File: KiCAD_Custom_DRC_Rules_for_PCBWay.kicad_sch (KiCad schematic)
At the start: 38 parts, among them J1 Screw_Terminal_01x02, J2 x2 OpAmp ZIF, J3 x1 OpAmp ZIF, J4 x4 OpAmp ZIF, U1 TL072

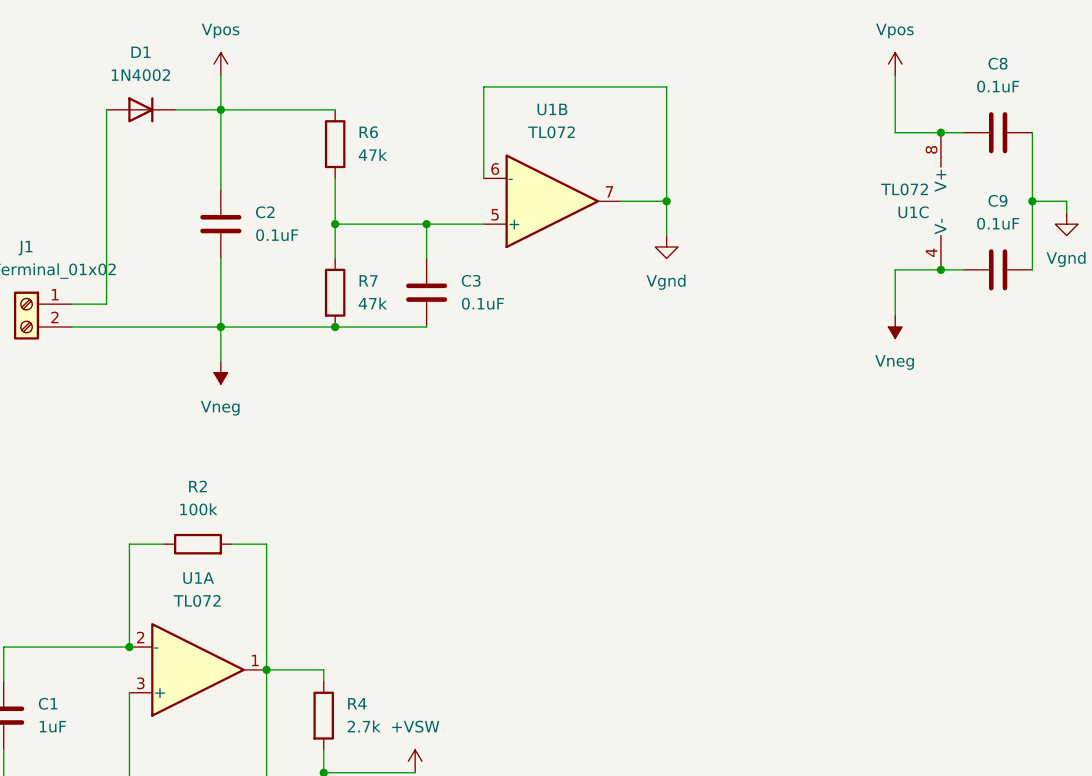
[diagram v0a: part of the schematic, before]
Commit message: cleanup, datasheet updates, add BOM
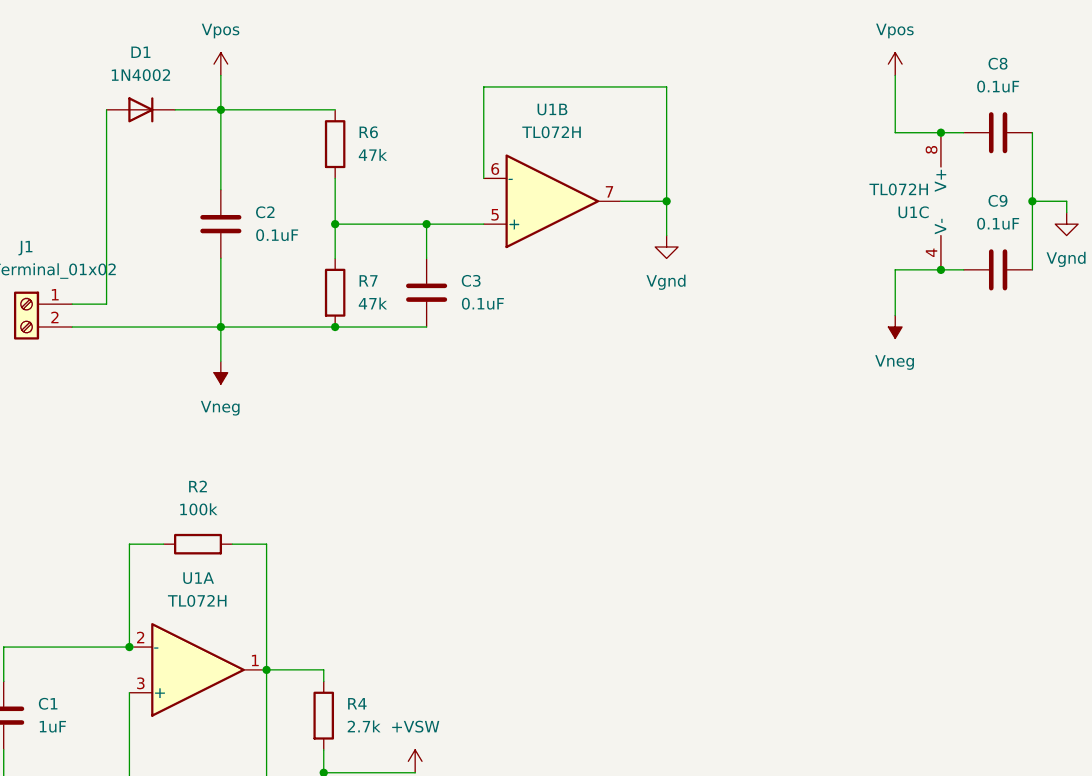
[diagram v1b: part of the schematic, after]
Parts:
- U1: value TL072 -> TL072H
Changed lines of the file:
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@@
 			)
 		)
-		(property "Value" "TL072"
+		(property "Value" "TL072H"
 			(at 82.55 26.67 0)
 			(effects
@@
 			)
 		)
-		(property "Datasheet" "http://www.ti.com/lit/ds/symlink/tl071.pdf"
+		(property "Datasheet" "https://www.ti.com/lit/ds/symlink/tl072h.pdf"
 			(at 82.55 34.29 0)
 			(effects
@@
 			)
 		)
-		(property "Value" "TL072"
+		(property "Value" "TL072H"
 			(at 124.46 33.0201 0)
 			(effects
@@
 			)
 		)
-		(property "Datasheet" "http://www.ti.com/lit/ds/symlink/tl071.pdf"
+		(property "Datasheet" "https://www.ti.com/lit/ds/symlink/tl072h.pdf"
 			(at 128.27 34.29 0)
 			(effects
@@
 			)
 		)
-		(property "Value" "TL072"
+		(property "Value" "TL072H"
 			(at 43.18 78.74 0)
 			(effects
@@
 			)
 		)
-		(property "Datasheet" "http://www.ti.com/lit/ds/symlink/tl071.pdf"
+		(property "Datasheet" "https://www.ti.com/lit/ds/symlink/tl072h.pdf"
 			(at 43.18 86.36 0)
 			(effects
